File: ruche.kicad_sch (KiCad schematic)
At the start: 30 parts, among them IC2 MAX17048G+, IC3 L86-M33, IC4 SHT41-AD1B-R3, J13 Micro_SD_Card, U1 MKRWAN_1310, U2 MS5611-01BA, U3 XC6220B331MR

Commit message: Correction cartouche schéma
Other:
- title: Testboard V2.3 -> Open_beehive_scale_board
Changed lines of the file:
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@@
   (paper "A4")
   (title_block
-    (title "Testboard V2.3")
-    (date "2021-12-11")
-    (rev "V0.2")
+    (title "Open_beehive_scale_board")
+    (date "2022-05-09")
+    (rev "V0.1")
     (company "Ratamuse")
   )

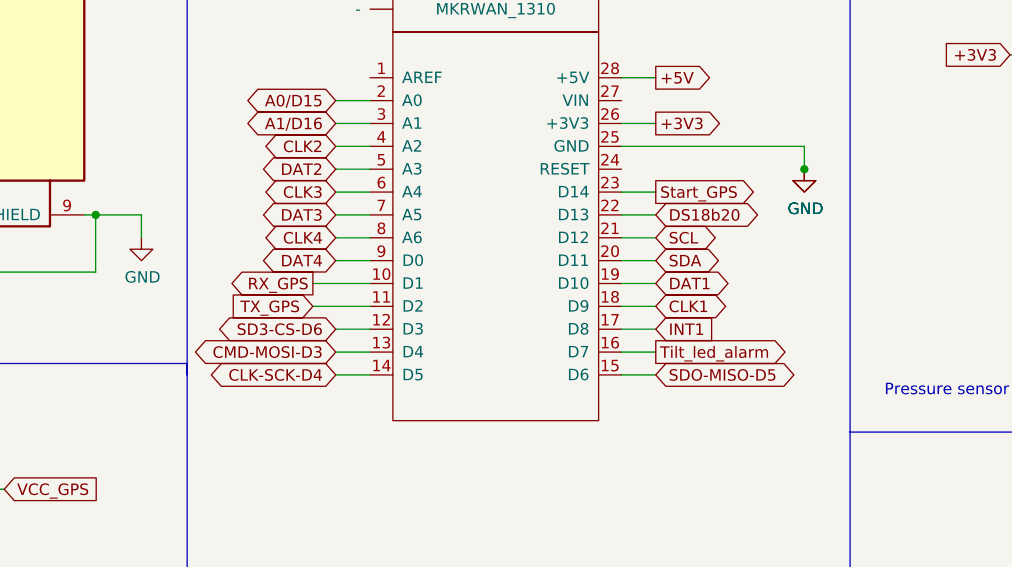
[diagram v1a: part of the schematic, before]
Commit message: Changement des pins
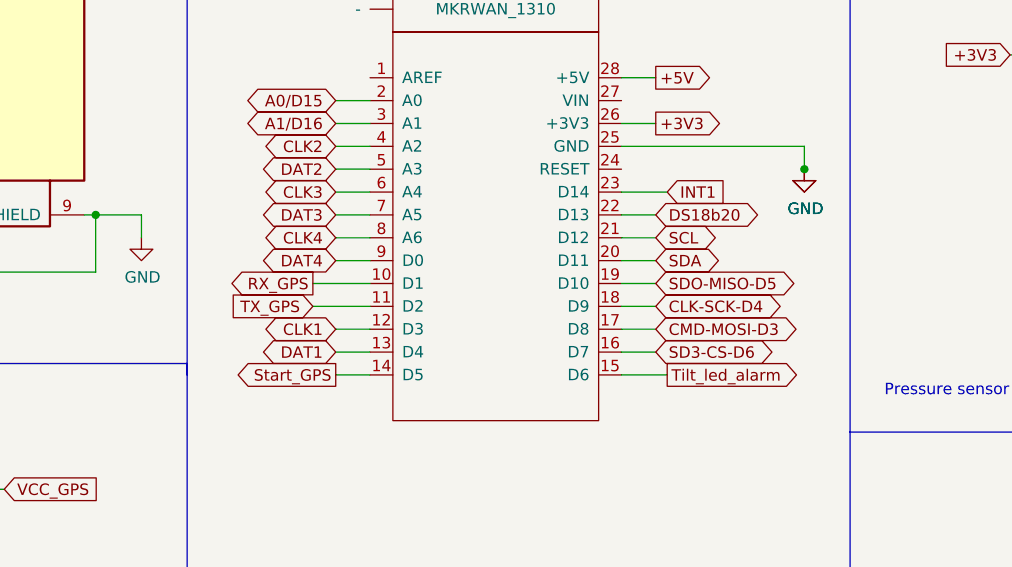
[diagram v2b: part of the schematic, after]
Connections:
- net CLK-SCK-D4: now also U1.18 (D9); no longer U1.14 (D5)
- net CLK1: now also U1.12 (D3); no longer U1.18 (D9)
- net CMD-MOSI-D3: now also U1.17 (D8); no longer U1.13 (D4)
- net DAT1: now also U1.13 (D4); no longer U1.19 (D10)
- net INT1: now also U1.23 (D14); no longer U1.17 (D8)
- net SD3-CS-D6: now also U1.16 (D7); no longer U1.12 (D3)
- net SDO-MISO-D5: now also U1.19 (D10); no longer U1.15 (D6)
- net Start_GPS: now also U1.14 (D5); no longer U1.23 (D14)
- net Tilt_led_alarm: now also U1.15 (D6); no longer U1.16 (D7)

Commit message: Modification routage
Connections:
- net CLK-SCK-D4 renamed CLK-SCK-D9
- net CMD-MOSI-D3 renamed CMD-MOSI-D8
- net SD3-CS-D6 renamed SD3-CS-D7
- net SDO-MISO-D5 renamed SDO-MISO-D10
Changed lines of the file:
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@@
     )
   )
-  (global_label "SD3-CS-D6" (shape bidirectional) (at 175.26 111.76 0) (fields_autoplaced)
+  (global_label "SD3-CS-D7" (shape bidirectional) (at 175.26 111.76 0) (fields_autoplaced)
     (effects (font (size 1.27 1.27)) (justify left))
     (property "Intersheet References" "${INTERSHEET_REFS}" (id 0) (at 189.3771 111.6806 0)
@@
     )
   )
-  (global_label "SD3-CS-D6" (shape bidirectional) (at 30.48 76.2 180) (fields_autoplaced)
+  (global_label "SD3-CS-D7" (shape bidirectional) (at 30.48 76.2 180) (fields_autoplaced)
     (effects (font (size 1.27 1.27)) (justify right))
     (property "Intersheet References" "${INTERSHEET_REFS}" (id 0) (at 16.3629 76.1206 0)
@@
     )
   )
-  (global_label "CLK-SCK-D4" (shape bidirectional) (at 30.48 83.82 180) (fields_autoplaced)
+  (global_label "CLK-SCK-D9" (shape bidirectional) (at 30.48 83.82 180) (fields_autoplaced)
     (effects (font (size 1.27 1.27)) (justify right))
     (property "Intersheet References" "${INTERSHEET_REFS}" (id 0) (at 15.2139 83.7406 0)
@@
     )
   )
-  (global_label "SDO-MISO-D5" (shape bidirectional) (at 175.26 104.14 0) (fields_autoplaced)
-    (effects (font (size 1.27 1.27)) (justify left))
-    (property "Intersheet References" "${INTERSHEET_REFS}" (id 0) (at 191.6147 104.0606 0)
+  (global_label "SDO-MISO-D10" (shape bidirectional) (at 175.26 104.14 0) (fields_autoplaced)
+    (effects (font (size 1.27 1.27)) (justify left))
+    (property "Intersheet References" "${INTERSHEET_REFS}" (id 0) (at 192.8242 104.0606 0)
       (effects (font (size 1.27 1.27)) (justify left) hide)
     )
@@
     )
   )
-  (global_label "CLK-SCK-D4" (shape bidirectional) (at 175.26 106.68 0) (fields_autoplaced)
+  (global_label "CLK-SCK-D9" (shape bidirectional) (at 175.26 106.68 0) (fields_autoplaced)
     (effects (font (size 1.27 1.27)) (justify left))
     (property "Intersheet References" "${INTERSHEET_REFS}" (id 0) (at 190.5261 106.6006 0)
@@
     )
   )
-  (global_label "CMD-MOSI-D3" (shape bidirectional) (at 175.26 109.22 0) (fields_autoplaced)
+  (global_label "CMD-MOSI-D8" (shape bidirectional) (at 175.26 109.22 0) (fields_autoplaced)
     (effects (font (size 1.27 1.27)) (justify left))
     (property "Intersheet References" "${INTERSHEET_REFS}" (id 0) (at 191.7961 109.1406 0)
@@
     )
   )
-  (global_label "CMD-MOSI-D3" (shape bidirectional) (at 30.48 78.74 180) (fields_autoplaced)
+  (global_label "CMD-MOSI-D8" (shape bidirectional) (at 30.48 78.74 180) (fields_autoplaced)
     (effects (font (size 1.27 1.27)) (justify right))
     (property "Intersheet References" "${INTERSHEET_REFS}" (id 0) (at 13.9439 78.6606 0)
@@
     )
   )
-  (global_label "SDO-MISO-D5" (shape bidirectional) (at 30.48 88.9 180) (fields_autoplaced)
-    (effects (font (size 1.27 1.27)) (justify right))
-    (property "Intersheet References" "${INTERSHEET_REFS}" (id 0) (at 14.1253 88.8206 0)
-      (effects (font (size 1.27 1.27)) (justify right) hide)
-    )
+  (global_label "SDO-MISO-D10" (shape bidirectional) (at 30.48 88.9 180) (fields_autoplaced)
+    (effects (font (size 1.27 1.27)) (justify right))
+    (property "Intersheet References" "${INTERSHEET_REFS}" (id 0) (at 12.9158 88.8206 0)
+      (effects (font (size 1.27 1.27)) (justify right) hide)
+    )

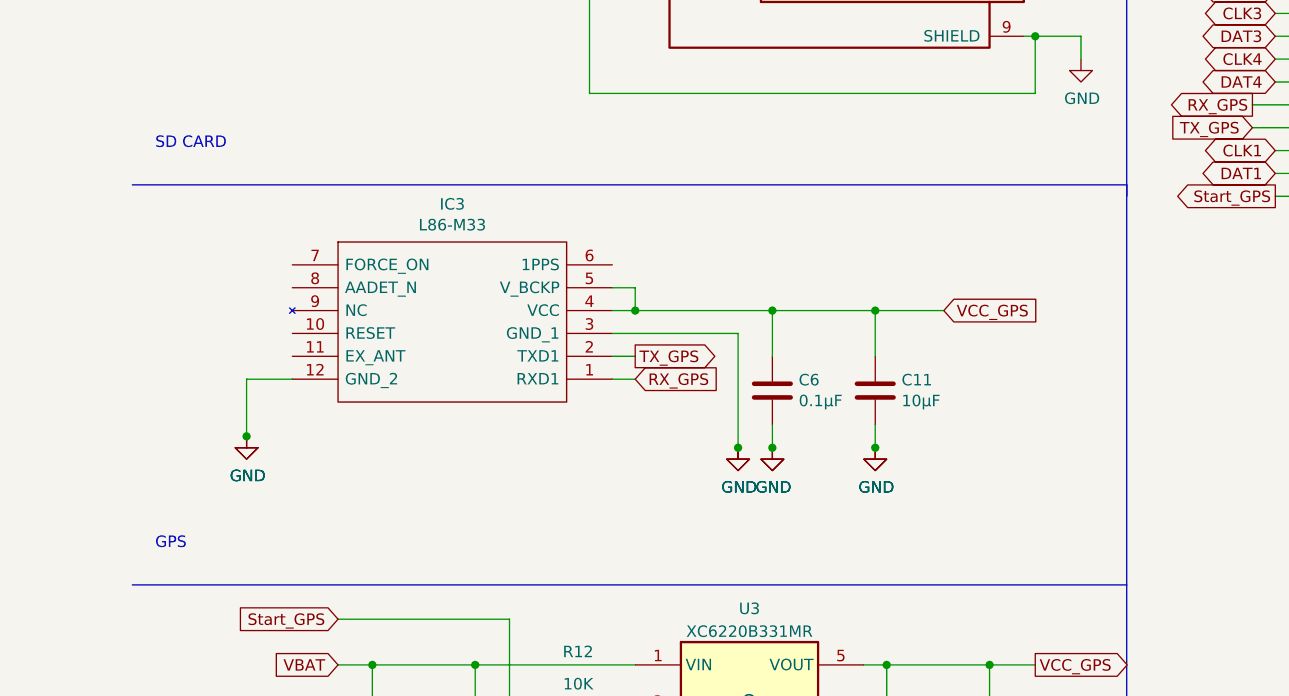
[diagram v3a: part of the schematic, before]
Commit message: Add GPS backup power supply
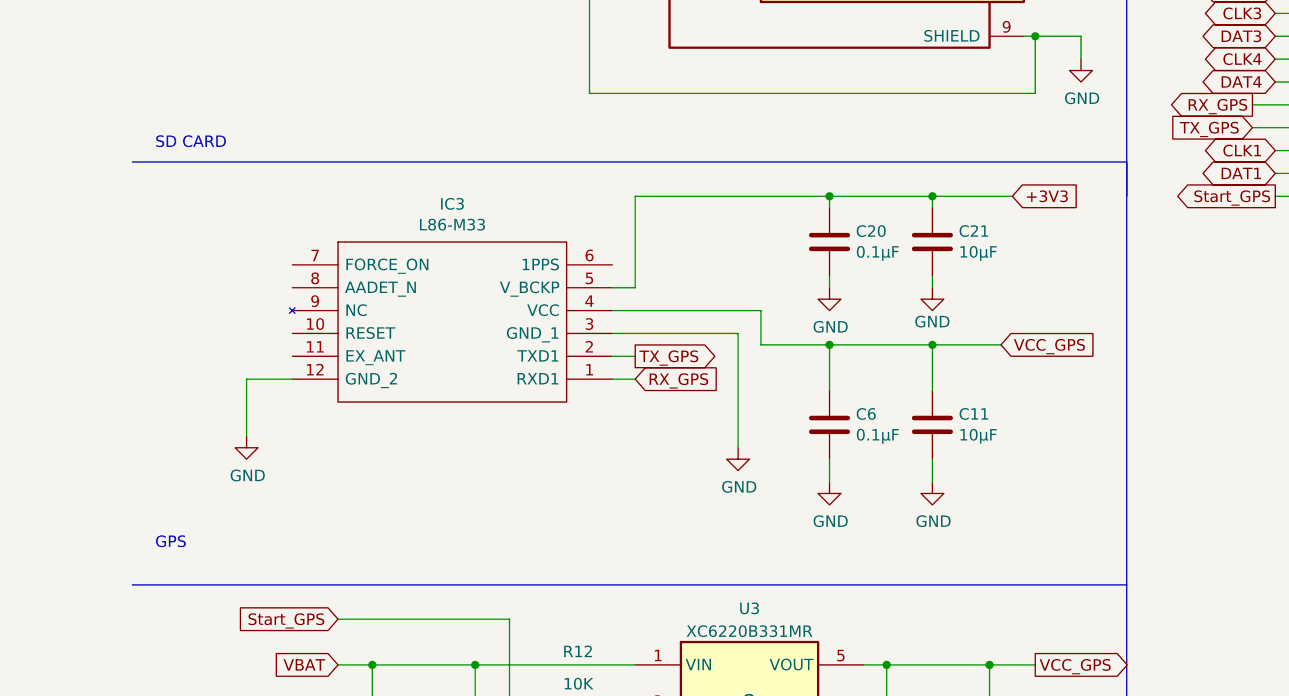
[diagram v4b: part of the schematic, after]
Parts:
- added C20: 0.1µF, Capacitor_SMD:C_0603_1608Metric, symbol Device:C
- added C21: 10µF, Capacitor_SMD:C_0805_2012Metric, symbol Device:C
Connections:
- net +3V3: now also IC3.5 (V_BCKP), C20.1, C21.1
- net GND: now also C20.2, C21.2
- net VCC_GPS: no longer IC3.5 (V_BCKP)
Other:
- moved on the sheet: C11, C6

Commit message: Add graphics
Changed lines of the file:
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@@
     (pin "2")
   )
-  (sheet (at 0 215.9) (size 77.47 58.42) (fields_autoplaced)
+  (sheet (at 0 215.9) (size 297.18 92.71) (fields_autoplaced)
     (stroke (width 0) (type solid) (color 0 0 0 0))
     (fill (color 0 0 0 0.0000))
@@
       (effects (font (size 1.27 1.27)) (justify left bottom))
     )
-    (property "Sheet file" "ruchea.kicad_sch" (id 1) (at 0 274.9046 0)
+    (property "Sheet file" "ruchea.kicad_sch" (id 1) (at 0 309.1946 0)
       (effects (font (size 1.27 1.27)) (justify left top))
     )
   )
-  (sheet (at 0 289.56) (size 101.6 64.77) (fields_autoplaced)
+  (sheet (at 0 320.04) (size 297.18 134.62) (fields_autoplaced)
     (stroke (width 0) (type solid) (color 0 0 0 0))
     (fill (color 0 0 0 0.0000))
-    (property "Sheet name" "rucheb" (id 0) (at 0 288.8484 0)
+    (property "Sheet name" "rucheb" (id 0) (at 0 319.3284 0)
       (effects (font (size 1.27 1.27)) (justify left bottom))
     )
-    (property "Sheet file" "rucheb.kicad_sch" (id 1) (at 0 354.9146 0)
+    (property "Sheet file" "rucheb.kicad_sch" (id 1) (at 0 455.2446 0)
       (effects (font (size 1.27 1.27)) (justify left top))
     )

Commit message: V0.2
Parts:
- added FID1, FID2, FID3, FID4: Fiducial, Fiducial:Fiducial_1mm_Mask3mm, symbol Mechanical:Fiducial
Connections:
- net DS18b20: now also U1.11 (D2); no longer U1.22 (D13)
- net INT1: now also U1.10 (D1); no longer U1.23 (D14)
- net RX_GPS: now also U1.23 (D14); no longer U1.10 (D1)
- net SCL: now also U2.8 (SCLK); no longer U2.7 (SDI/SDA)
- net SDA: now also U2.7 (SDI/SDA); no longer U2.8 (SCLK)
- net TX_GPS: now also U1.22 (D13); no longer U1.11 (D2)
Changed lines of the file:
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@@
+    (stroke (width 0) (type default) (color 0 0 0 0))
+  )
+  (wire (pts (xy 139.7 106.68) (xy 143.51 106.68))
     (stroke (width 0) (type default) (color 0 0 0 0))
   )
@@
     (stroke (width 0) (type default) (color 0 0 0 0))
   )
+  (wire (pts (xy 171.45 93.98) (xy 175.26 93.98))
+    (stroke (width 0) (type default) (color 0 0 0 0))
+  )
   (wire (pts (xy 237.49 140.97) (xy 237.49 147.32))
     (stroke (width 0) (type default) (color 0 0 0 0))
@@
     (stroke (width 0) (type default) (color 0 0 0 0))
   )
-  (wire (pts (xy 137.16 106.68) (xy 143.51 106.68))
-    (stroke (width 0) (type default) (color 0 0 0 0))
-  )
   (wire (pts (xy 85.09 26.67) (xy 85.09 40.64))
     (stroke (width 0) (type default) (color 0 0 0 0))
@@
     (stroke (width 0) (type default) (color 0 0 0 0))
   )
+  (wire (pts (xy 139.7 104.14) (xy 143.51 104.14))
+    (stroke (width 0) (type default) (color 0 0 0 0))
+  )
   (wire (pts (xy 81.28 179.07) (xy 81.28 181.61))
     (stroke (width 0) (type default) (color 0 0 0 0))
@@
     (stroke (width 0) (type default) (color 0 0 0 0))
   )
-  (wire (pts (xy 175.26 96.52) (xy 171.45 96.52))
-    (stroke (width 0) (type default) (color 0 0 0 0))
-  )
   (wire (pts (xy 252.73 156.21) (xy 260.35 156.21))
     (stroke (width 0) (type default) (color 0 0 0 0))
@@
     (stroke (width 0) (type default) (color 0 0 0 0))
   )
-  (wire (pts (xy 171.45 93.98) (xy 176.53 93.98))
-    (stroke (width 0) (type default) (color 0 0 0 0))
-  )
   (wire (pts (xy 171.45 109.22) (xy 175.26 109.22))
     (stroke (width 0) (type default) (color 0 0 0 0))
@@
     (stroke (width 0) (type default) (color 0 0 0 0))
   )
+  (wire (pts (xy 171.45 96.52) (xy 175.26 96.52))
+    (stroke (width 0) (type default) (color 0 0 0 0))
+  )
   (wire (pts (xy 266.7 85.09) (xy 266.7 82.55))
     (stroke (width 0) (type default) (color 0 0 0 0))
@@
   )
   (wire (pts (xy 53.34 58.42) (xy 53.34 62.23))
-    (stroke (width 0) (type default) (color 0 0 0 0))
-  )
-  (wire (pts (xy 137.16 104.14) (xy 143.51 104.14))
     (stroke (width 0) (type default) (color 0 0 0 0))
   )
@@
     )
   )
-  (global_label "SCL" (shape bidirectional) (at 243.84 95.25 180) (fields_autoplaced)
-    (effects (font (size 1.27 1.27)) (justify right))
-    (property "Intersheet References" "${INTERSHEET_REFS}" (id 0) (at -3.81 -5.08 0)
-      (effects (font (size 1.27 1.27)) hide)
+  (global_label "SDA" (shape bidirectional) (at 243.84 95.25 180) (fields_autoplaced)
+    (effects (font (size 1.27 1.27)) (justify right))
+    (property "Intersheet References" "${INTERSHEET_REFS}" (id 0) (at 237.9477 95.1706 0)
+      (effects (font (size 1.27 1.27)) (justify right) hide)
     )
   )
@@
     )
   )
-  (global_label "DS18b20" (shape bidirectional) (at 175.26 96.52 0) (fields_autoplaced)
-    (effects (font (size 1.27 1.27)) (justify left))
-    (property "Intersheet References" "${INTERSHEET_REFS}" (id 0) (at 113.03 48.26 0)
-      (effects (font (size 1.27 1.27)) hide)
+  (global_label "DS18b20" (shape bidirectional) (at 139.7 106.68 180) (fields_autoplaced)
+    (effects (font (size 1.27 1.27)) (justify right))
+    (property "Intersheet References" "${INTERSHEET_REFS}" (id 0) (at 128.9091 106.6006 0)
+      (effects (font (size 1.27 1.27)) (justify right) hide)
     )
   )
@@
     )
   )
-  (global_label "TX_GPS" (shape input) (at 137.16 106.68 180) (fields_autoplaced)
-    (effects (font (size 1.27 1.27)) (justify right))
-    (property "Intersheet References" "${INTERSHEET_REFS}" (id 0) (at 113.03 48.26 0)
-      (effects (font (size 1.27 1.27)) hide)
+  (global_label "TX_GPS" (shape input) (at 175.26 96.52 0) (fields_autoplaced)
+    (effects (font (size 1.27 1.27)) (justify left))
+    (property "Intersheet References" "${INTERSHEET_REFS}" (id 0) (at 184.4785 96.4406 0)
+      (effects (font (size 1.27 1.27)) (justify left) hide)
     )
   )
@@
     )
   )
-  (global_label "INT1" (shape input) (at 176.53 93.98 0) (fields_autoplaced)
-    (effects (font (size 1.27 1.27)) (justify left))
-    (property "Intersheet References" "${INTERSHEET_REFS}" (id 0) (at 182.9666 93.9006 0)
-      (effects (font (size 1.27 1.27)) (justify left) hide)
+  (global_label "INT1" (shape input) (at 139.7 104.14 180) (fields_autoplaced)
+    (effects (font (size 1.27 1.27)) (justify right))
+    (property "Intersheet References" "${INTERSHEET_REFS}" (id 0) (at 133.2634 104.0606 0)
+      (effects (font (size 1.27 1.27)) (justify right) hide)
     )
   )
@@
     )
   )
-  (global_label "RX_GPS" (shape output) (at 137.16 104.14 180) (fields_autoplaced)
-    (effects (font (size 1.27 1.27)) (justify right))
-    (property "Intersheet References" "${INTERSHEET_REFS}" (id 0) (at 113.03 48.26 0)
-      (effects (font (size 1.27 1.27)) hide)
+  (global_label "RX_GPS" (shape output) (at 175.26 93.98 0) (fields_autoplaced)
+    (effects (font (size 1.27 1.27)) (justify left))
+    (property "Intersheet References" "${INTERSHEET_REFS}" (id 0) (at 184.7809 93.9006 0)
+      (effects (font (size 1.27 1.27)) (justify left) hide)
     )
   )
@@
     )
   )
-  (global_label "SDA" (shape bidirectional) (at 243.84 97.79 180) (fields_autoplaced)
-    (effects (font (size 1.27 1.27)) (justify right))
-    (property "Intersheet References" "${INTERSHEET_REFS}" (id 0) (at -3.81 -5.08 0)
-      (effects (font (size 1.27 1.27)) hide)
+  (global_label "SCL" (shape bidirectional) (at 243.84 97.79 180) (fields_autoplaced)
+    (effects (font (size 1.27 1.27)) (justify right))
+    (property "Intersheet References" "${INTERSHEET_REFS}" (id 0) (at 238.0082 97.7106 0)
+      (effects (font (size 1.27 1.27)) (justify right) hide)
     )
   )
@@
     (pin "2")
   )
+  (symbol (lib_id "Mechanical:Fiducial") (at 135.89 157.48 0) (unit 1)
+    (in_bom yes) (on_board yes) (fields_autoplaced)
+    (property "Reference" "FID2" (id 0) (at 138.049 156.6453 0)
+      (effects (font (size 1.27 1.27)) (justify left))
+    )
+    (property "Value" "Fiducial" (id 1) (at 138.049 159.1822 0)
+      (effects (font (size 1.27 1.27)) (justify left))
+    )
+    (property "Footprint" "Fiducial:Fiducial_1mm_Mask3mm" (id 2) (at 135.89 157.48 0)
+      (effects (font (size 1.27 1.27)) hide)
+    )
+    (property "Datasheet" "~" (id 3) (at 135.89 157.48 0)
+      (effects (font (size 1.27 1.27)) hide)
+    )
+  )
   (symbol (lib_id "Device:C") (at 232.41 83.82 0) (unit 1)
     (in_bom yes) (on_board yes)
@@
     (pin "1")
   )
+  (symbol (lib_id "Mechanical:Fiducial") (at 156.21 146.05 0) (unit 1)
+    (in_bom yes) (on_board yes) (fields_autoplaced)
+    (property "Reference" "FID3" (id 0) (at 158.369 145.2153 0)
+      (effects (font (size 1.27 1.27)) (justify left))
+    )
+    (property "Value" "Fiducial" (id 1) (at 158.369 147.7522 0)
+      (effects (font (size 1.27 1.27)) (justify left))
+    )
+    (property "Footprint" "Fiducial:Fiducial_1mm_Mask3mm" (id 2) (at 156.21 146.05 0)
+      (effects (font (size 1.27 1.27)) hide)
+    )
+    (property "Datasheet" "~" (id 3) (at 156.21 146.05 0)
+      (effects (font (size 1.27 1.27)) hide)
+    )
+  )
   (symbol (lib_id "Device:R") (at 44.45 66.04 0) (unit 1)
     (in_bom yes) (on_board yes)
@@
     (pin "1")
   )
+  (symbol (lib_id "Mechanical:Fiducial") (at 135.89 146.05 0) (unit 1)
+    (in_bom yes) (on_board yes) (fields_autoplaced)
+    (property "Reference" "FID1" (id 0) (at 138.049 145.2153 0)
+      (effects (font (size 1.27 1.27)) (justify left))
+    )
+    (property "Value" "Fiducial" (id 1) (at 138.049 147.7522 0)
+      (effects (font (size 1.27 1.27)) (justify left))
+    )
+    (property "Footprint" "Fiducial:Fiducial_1mm_Mask3mm" (id 2) (at 135.89 146.05 0)
+      (effects (font (size 1.27 1.27)) hide)
+    )
+    (property "Datasheet" "~" (id 3) (at 135.89 146.05 0)
+      (effects (font (size 1.27 1.27)) hide)
+    )
+  )
   (symbol (lib_id "power:GND") (at 266.7 110.49 0) (unit 1)
     (in_bom yes) (on_board yes)
@@
     )
     (pin "1")
+  )
+  (symbol (lib_id "Mechanical:Fiducial") (at 156.21 157.48 0) (unit 1)
+    (in_bom yes) (on_board yes) (fields_autoplaced)
+    (property "Reference" "FID4" (id 0) (at 158.369 156.6453 0)
+      (effects (font (size 1.27 1.27)) (justify left))
+    )
+    (property "Value" "Fiducial" (id 1) (at 158.369 159.1822 0)
+      (effects (font (size 1.27 1.27)) (justify left))
+    )
+    (property "Footprint" "Fiducial:Fiducial_1mm_Mask3mm" (id 2) (at 156.21 157.48 0)
+      (effects (font (size 1.27 1.27)) hide)
+    )
+    (property "Datasheet" "~" (id 3) (at 156.21 157.48 0)
+      (effects (font (size 1.27 1.27)) hide)
+    )
   )
   (symbol (lib_id "power:GND") (at 118.11 99.06 0) (unit 1)
@@
       (reference "FB1") (unit 1) (value "FerriteBead") (footprint "Resistor_SMD:R_0603_1608Metric")
     )
+    (path "/86bdc510-c778-45e0-b037-11148ebcd2d4"
+      (reference "FID1") (unit 1) (value "Fiducial") (footprint "Fiducial:Fiducial_1mm_Mask3mm")
+    )
+    (path "/2c608864-e6af-45e6-811b-5efe3309d320"
+      (reference "FID2") (unit 1) (value "Fiducial") (footprint "Fiducial:Fiducial_1mm_Mask3mm")
+    )
+    (path "/7982a1f2-441d-4ddf-b0ba-97db71059f0f"
+      (reference "FID3") (unit 1) (value "Fiducial") (footprint "Fiducial:Fiducial_1mm_Mask3mm")
+    )
+    (path "/965affb2-c3f4-484e-9c0a-0b5682f1b69d"
+      (reference "FID4") (unit 1) (value "Fiducial") (footprint "Fiducial:Fiducial_1mm_Mask3mm")
+    )
     (path "/00000000-0000-0000-0000-0000609e7af1/31c6505b-fdd9-40cc-a280-26c0fa241def"
